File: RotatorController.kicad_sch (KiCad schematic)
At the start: 60 parts, among them J1 USB_A, J2 26 VAC, J3 Rotator, K1 G5LE-1, K2 G5LE-1, K3 G5LE-1, Q1 BSS123, Q2 BSS123, Q3 BSS123, SW1 SW_CW, SW2 SW_CCW, U1 Teensy4.0, U3 AP2161W

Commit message: Added files Update board outline based on measurements Moved connectors to new board outline
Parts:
- C2, C3, C4, C5, C6, C7, C8, C9: footprint Capacitor_SMD:C_1210_3225Metric_Pad1.33x2.70mm_HandSolder -> Capacitor_SMD:C_1206_3216Metric_Pad1.33x1.80mm_HandSolder
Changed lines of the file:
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@@
       (effects (font (size 1.27 1.27)) (justify left))
     )
-    (property "Footprint" "Capacitor_SMD:C_1210_3225Metric_Pad1.33x2.70mm_HandSolder" (at 222.5548 171.45 0)
+    (property "Footprint" "Capacitor_SMD:C_1206_3216Metric_Pad1.33x1.80mm_HandSolder" (at 222.5548 171.45 0)
       (effects (font (size 1.27 1.27)) hide)
     )
@@
       (effects (font (size 1.27 1.27)))
     )
-    (property "Footprint" "Capacitor_SMD:C_1210_3225Metric_Pad1.33x2.70mm_HandSolder" (at 241.3 211.1248 0)
+    (property "Footprint" "Capacitor_SMD:C_1206_3216Metric_Pad1.33x1.80mm_HandSolder" (at 241.3 211.1248 0)
       (effects (font (size 1.27 1.27)) hide)
     )
@@
       (effects (font (size 1.27 1.27)))
     )
-    (property "Footprint" "Capacitor_SMD:C_1210_3225Metric_Pad1.33x2.70mm_HandSolder" (at 241.3 177.4952 0)
+    (property "Footprint" "Capacitor_SMD:C_1206_3216Metric_Pad1.33x1.80mm_HandSolder" (at 241.3 177.4952 0)
       (effects (font (size 1.27 1.27)) hide)
     )
@@
       (effects (font (size 1.27 1.27)) (justify left))
     )
-    (property "Footprint" "Capacitor_SMD:C_1210_3225Metric_Pad1.33x2.70mm_HandSolder" (at 230.8352 171.45 0)
+    (property "Footprint" "Capacitor_SMD:C_1206_3216Metric_Pad1.33x1.80mm_HandSolder" (at 230.8352 171.45 0)
       (effects (font (size 1.27 1.27)) hide)
     )
@@
       (effects (font (size 1.27 1.27)))
     )
-    (property "Footprint" "Capacitor_SMD:C_1210_3225Metric_Pad1.33x2.70mm_HandSolder" (at 256.54 211.1248 0)
+    (property "Footprint" "Capacitor_SMD:C_1206_3216Metric_Pad1.33x1.80mm_HandSolder" (at 256.54 211.1248 0)
       (effects (font (size 1.27 1.27)) hide)
     )
@@
       (effects (font (size 1.27 1.27)) (justify left))
     )
-    (property "Footprint" "Capacitor_SMD:C_1210_3225Metric_Pad1.33x2.70mm_HandSolder" (at 230.8352 222.25 0)
+    (property "Footprint" "Capacitor_SMD:C_1206_3216Metric_Pad1.33x1.80mm_HandSolder" (at 230.8352 222.25 0)
       (effects (font (size 1.27 1.27)) hide)
     )
@@
       (effects (font (size 1.27 1.27)))
     )
-    (property "Footprint" "Capacitor_SMD:C_1210_3225Metric_Pad1.33x2.70mm_HandSolder" (at 254 175.5648 0)
+    (property "Footprint" "Capacitor_SMD:C_1206_3216Metric_Pad1.33x1.80mm_HandSolder" (at 254 175.5648 0)
       (effects (font (size 1.27 1.27)) hide)
     )
@@
       (effects (font (size 1.27 1.27)) (justify left))
     )
-    (property "Footprint" "Capacitor_SMD:C_1210_3225Metric_Pad1.33x2.70mm_HandSolder" (at 222.5548 222.25 0)
-      (effects (font (size 1.27 1.27)) hide)
-    )
+    (property "Footprint" "Capacitor_SMD:C_1206_3216Metric_Pad1.33x1.80mm_HandSolder" (at 222.5548 222.25 0)
+      (effects (font (size 1.27 1.27)) hide)
+    )

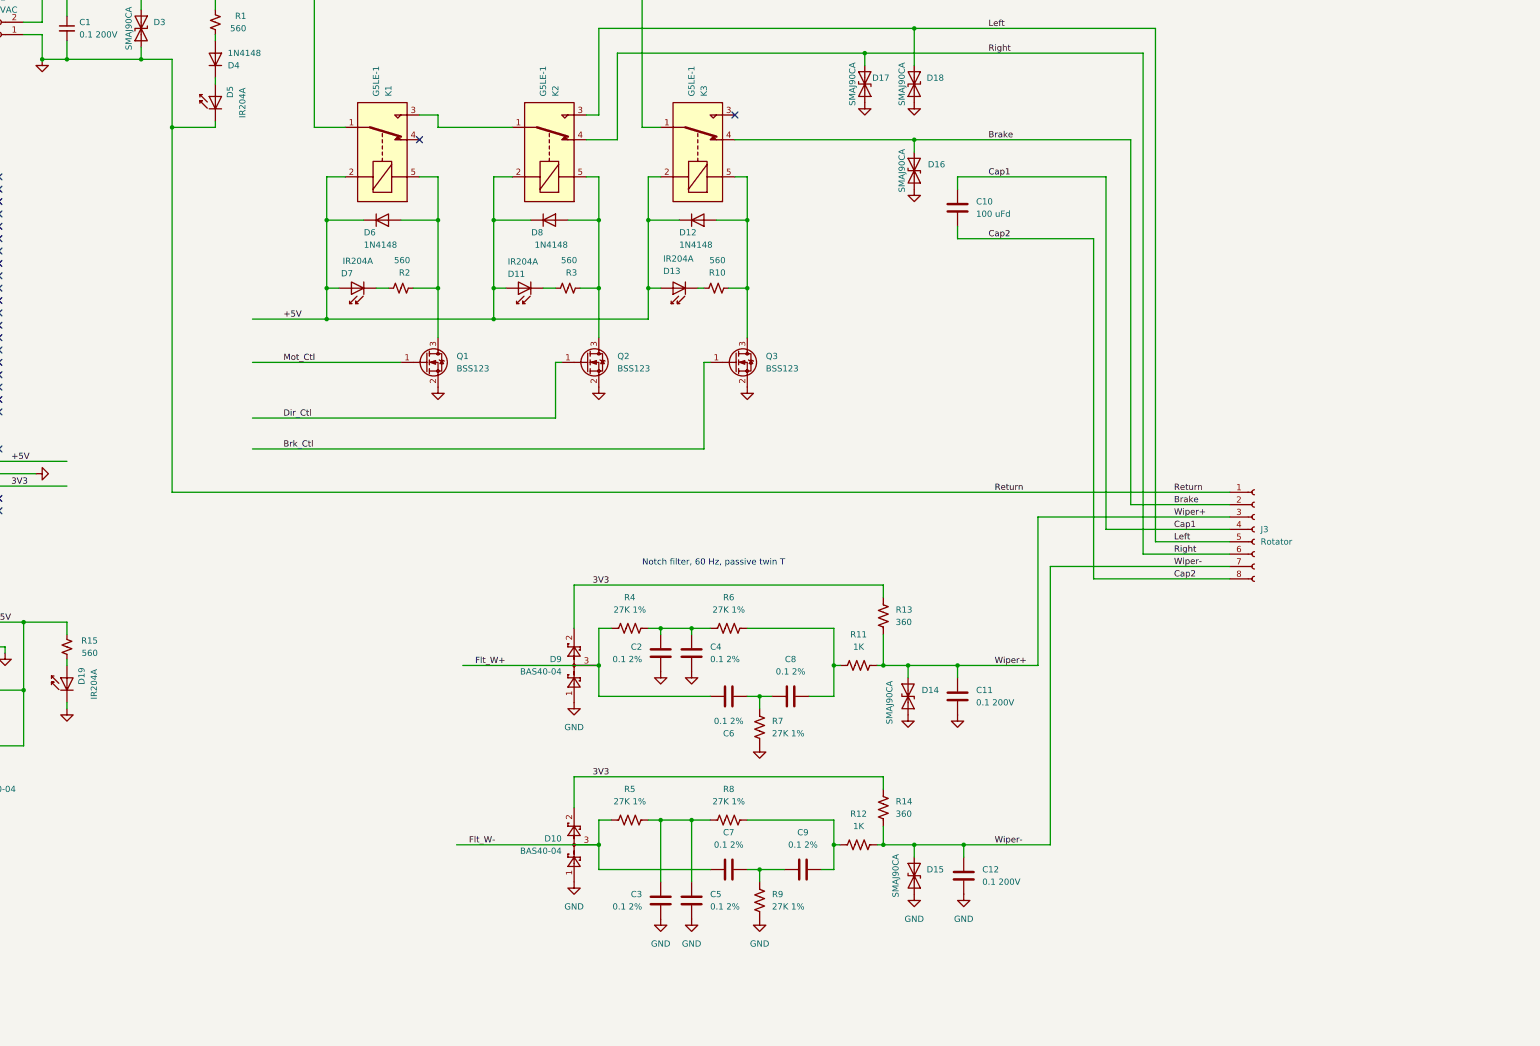
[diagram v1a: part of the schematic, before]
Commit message: Mid layout of smaller pcb with separately mounted cap still need to assign cap connector Added 4 high light pipe and 0805 LEDs, need to create footprint
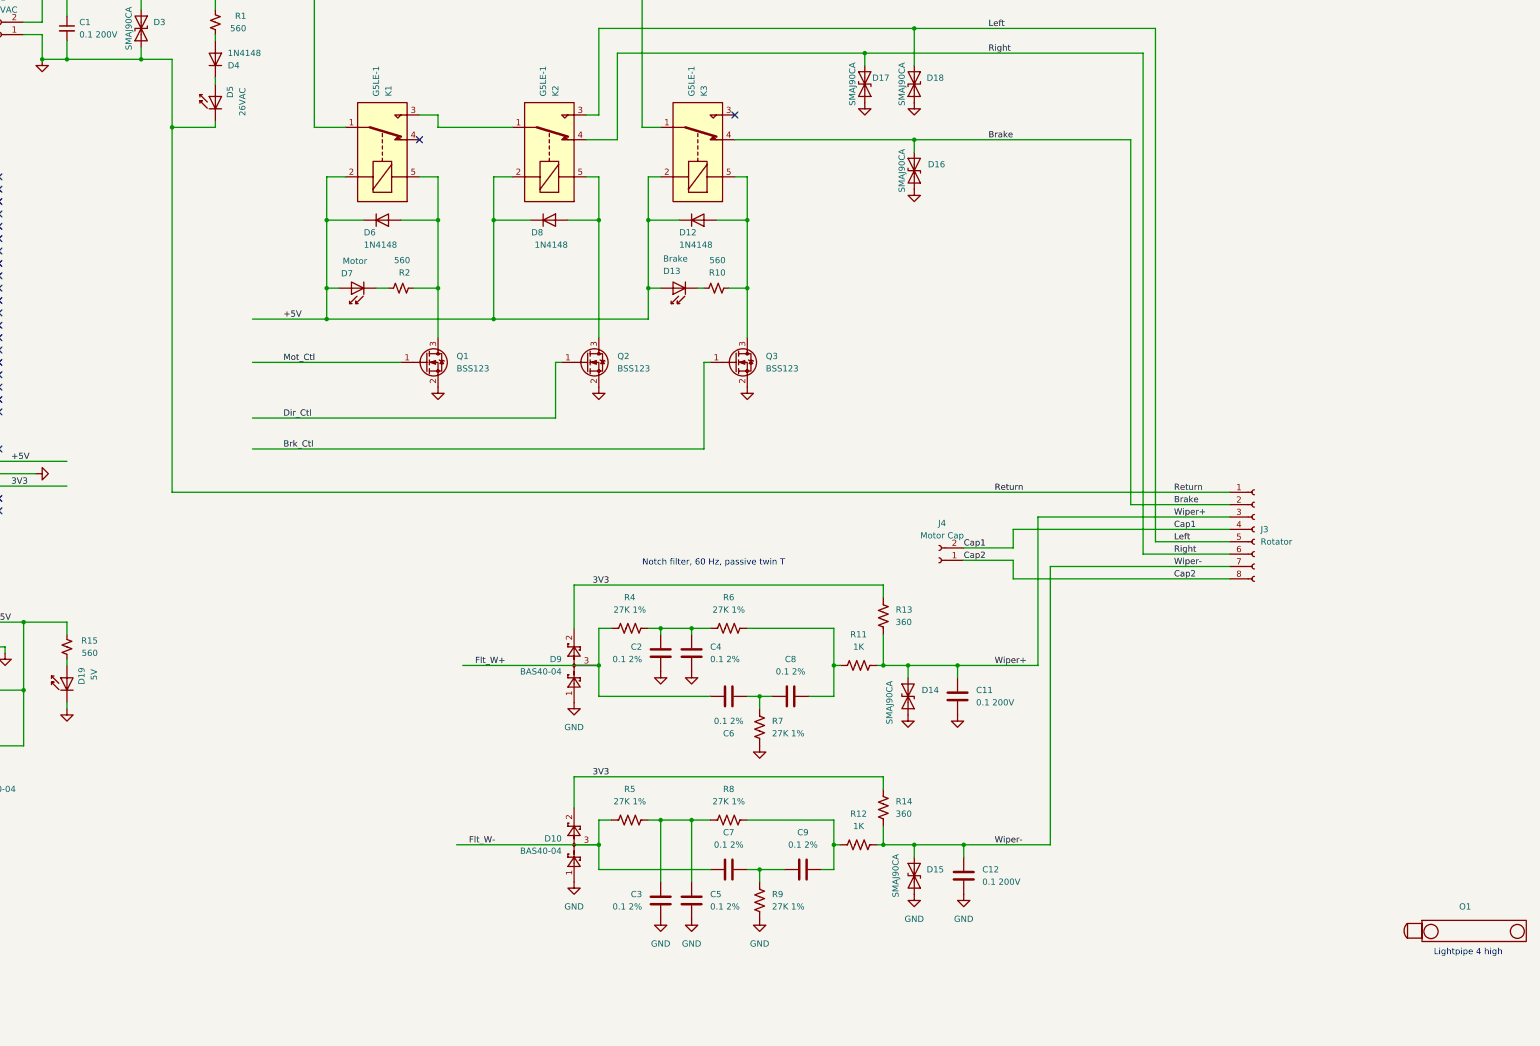
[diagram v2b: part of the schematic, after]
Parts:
- removed C10: 100 uFd, Capacitor_THT:C_Rect_L41.5mm_W20.0mm_P37.50mm_MKS4, symbol Device:C
- removed D11: IR204A, LED_THT:LED_D3.0mm_IRBlack, symbol LED:IR204A
- removed R3: 560, Resistor_SMD:R_0805_2012Metric_Pad1.20x1.40mm_HandSolder, symbol Device:R_Small_US
- added J4: Motor Cap, symbol Connector:Conn_01x02_Socket
- added O1: ~, symbol LightPipe:LP4-EP
- D13: value IR204A -> Brake; footprint LED_THT:LED_D3.0mm_IRBlack -> LED_SMD:LED_0603_1608Metric_Pad1.05x0.95mm_HandSolder
- D19: value IR204A -> 5V; footprint LED_THT:LED_D3.0mm_IRBlack -> LED_SMD:LED_0603_1608Metric_Pad1.05x0.95mm_HandSolder
- D5: value IR204A -> 26VAC; footprint LED_THT:LED_D3.0mm_IRBlack -> LED_SMD:LED_0603_1608Metric_Pad1.05x0.95mm_HandSolder
- D7: value IR204A -> Motor; footprint LED_THT:LED_D3.0mm_IRBlack -> LED_SMD:LED_0603_1608Metric_Pad1.05x0.95mm_HandSolder
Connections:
- net Cap1: now also J4.2 (Pin_2)
- net Cap2: now also J4.1 (Pin_1)
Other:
- note added: "Lightpipe 4 high"

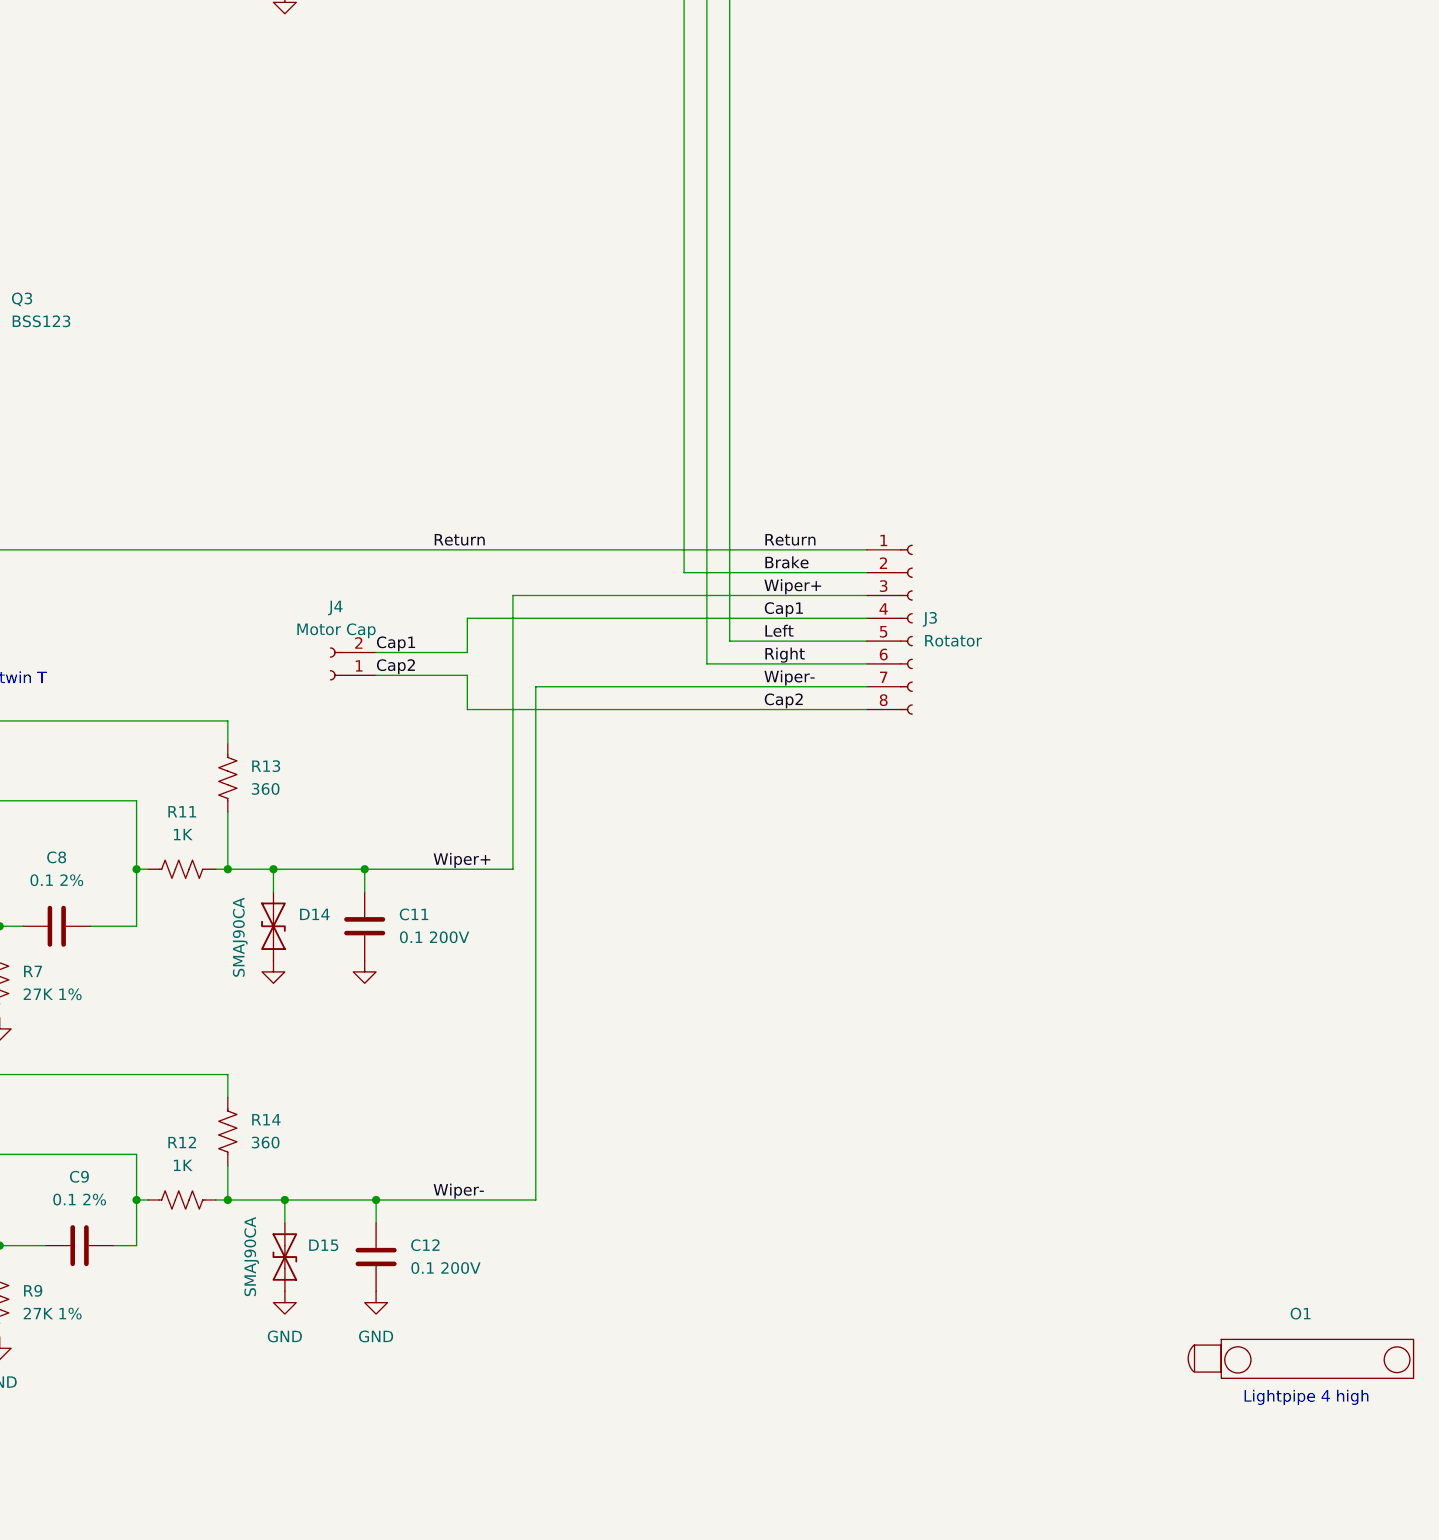
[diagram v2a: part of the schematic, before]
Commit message: Added light pipe footprint Completed layout and deisgn rule check
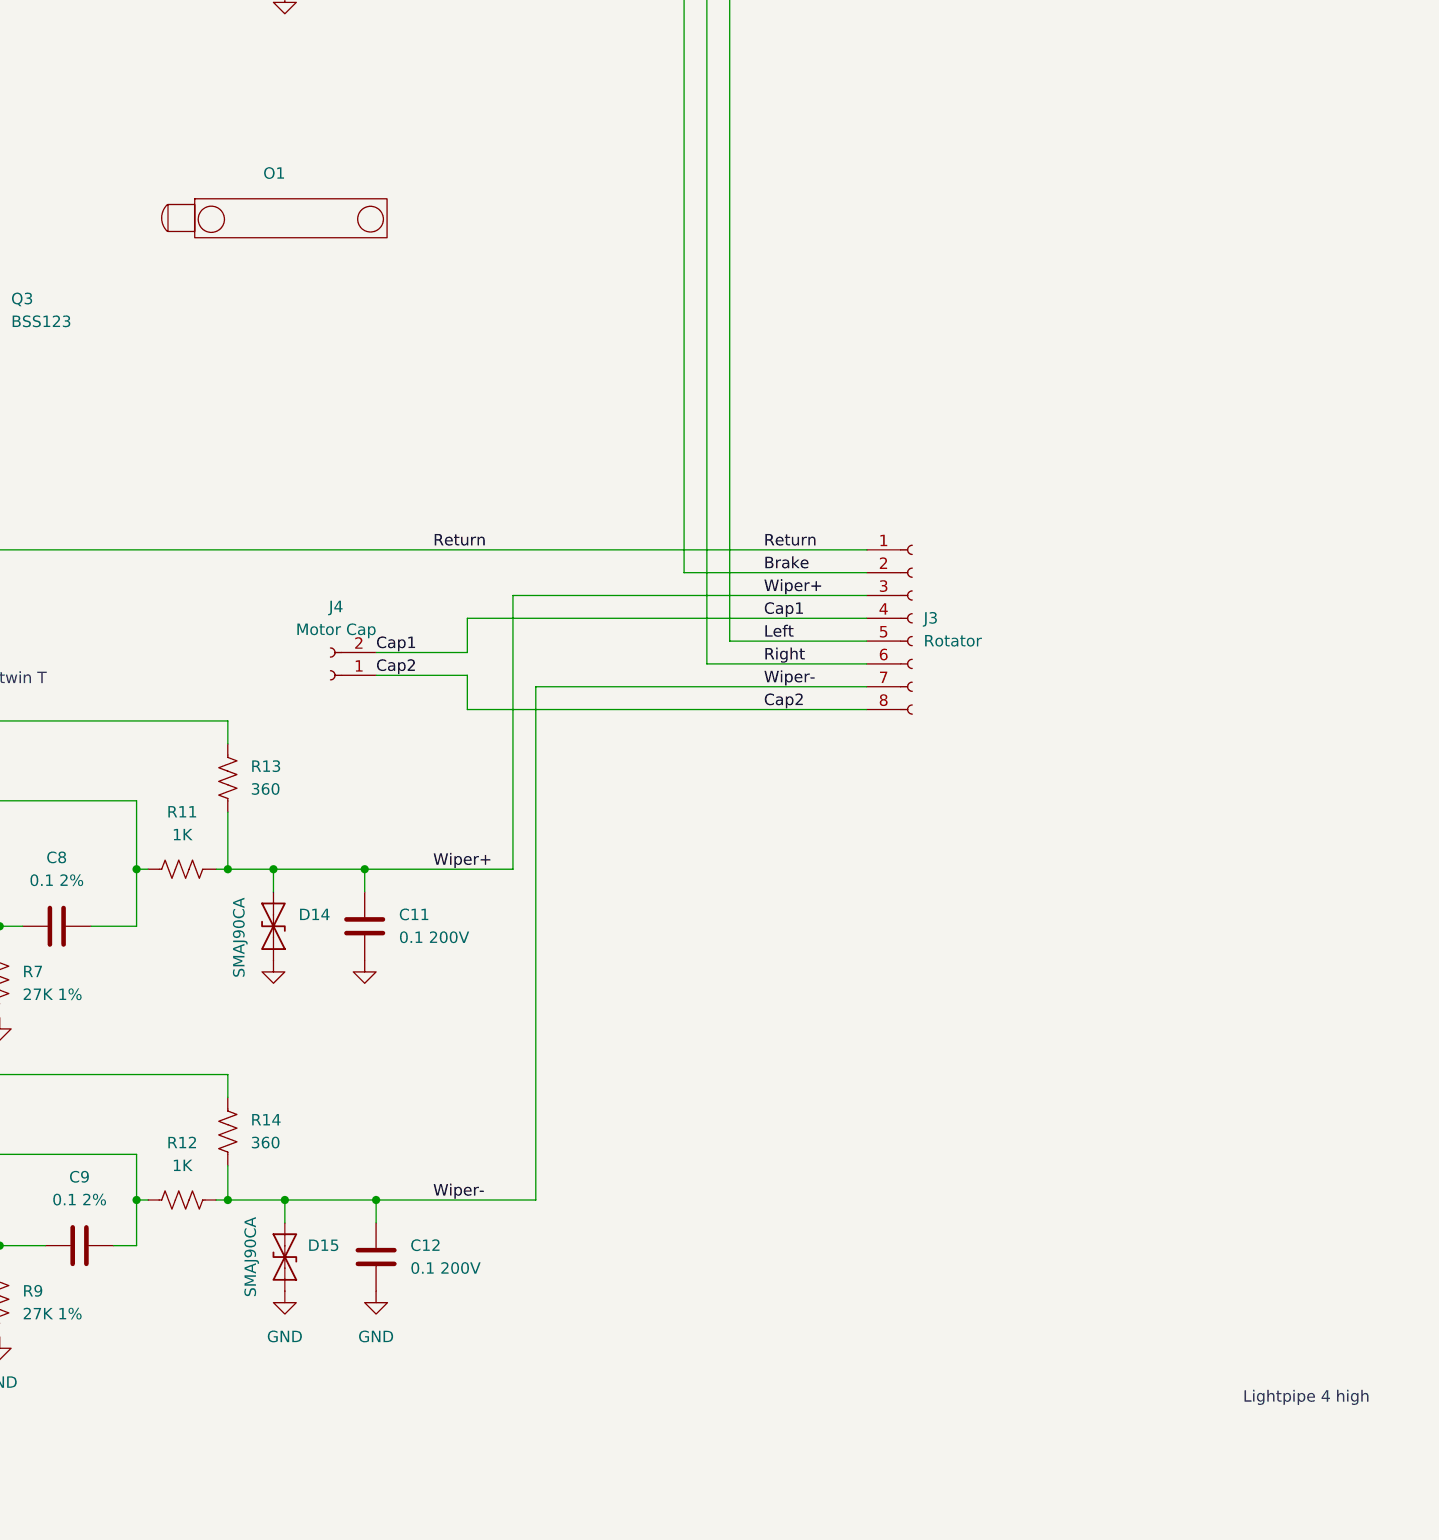
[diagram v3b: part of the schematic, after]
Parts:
- J4: footprint (none) -> Connector_PinHeader_2.54mm:PinHeader_1x02_P2.54mm_Vertical
- O1: footprint (none) -> Lightpipe:LP4-EP
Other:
- moved on the sheet: O1
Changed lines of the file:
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@@
       (effects (font (size 1.27 1.27)))
     )
-    (property "Footprint" "" (at 280.67 148.59 0)
+    (property "Footprint" "Connector_PinHeader_2.54mm:PinHeader_1x02_P2.54mm_Vertical" (at 280.67 148.59 0)
       (effects (font (size 1.27 1.27)) hide)
     )
@@
     )
   )
-  (symbol (lib_id "LightPipe:LP4-EP") (at 402.59 224.79 0) (unit 1)
-    (in_bom yes) (on_board yes) (dnp no) (fields_autoplaced)
-    (property "Reference" "O1" (at 388.7185 219.71 0)
-      (effects (font (size 1.27 1.27)))
-    )
-    (property "Value" "~" (at 402.59 224.79 0)
-      (effects (font (size 1.27 1.27)))
-    )
-    (property "Footprint" "" (at 402.59 224.79 0)
-      (effects (font (size 1.27 1.27)) hide)
-    )
-    (property "Datasheet" "" (at 402.59 224.79 0)
-      (effects (font (size 1.27 1.27)) hide)
-    )
+  (symbol (lib_id "LightPipe:LP4-EP") (at 288.29 97.79 0) (unit 1)
+    (in_bom yes) (on_board yes) (dnp no) (fields_autoplaced)
+    (property "Reference" "O1" (at 274.4185 92.71 0)
+      (effects (font (size 1.27 1.27)))
+    )
+    (property "Value" "~" (at 288.29 97.79 0)
+      (effects (font (size 1.27 1.27)))
+    )
+    (property "Footprint" "Lightpipe:LP4-EP" (at 288.29 97.79 0)
+      (effects (font (size 1.27 1.27)) hide)
+    )
+    (property "Datasheet" "" (at 288.29 97.79 0)
+      (effects (font (size 1.27 1.27)) hide)
+    )
